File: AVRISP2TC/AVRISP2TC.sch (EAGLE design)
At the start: 14 parts, among them U1 NCP1117LPST33T3G

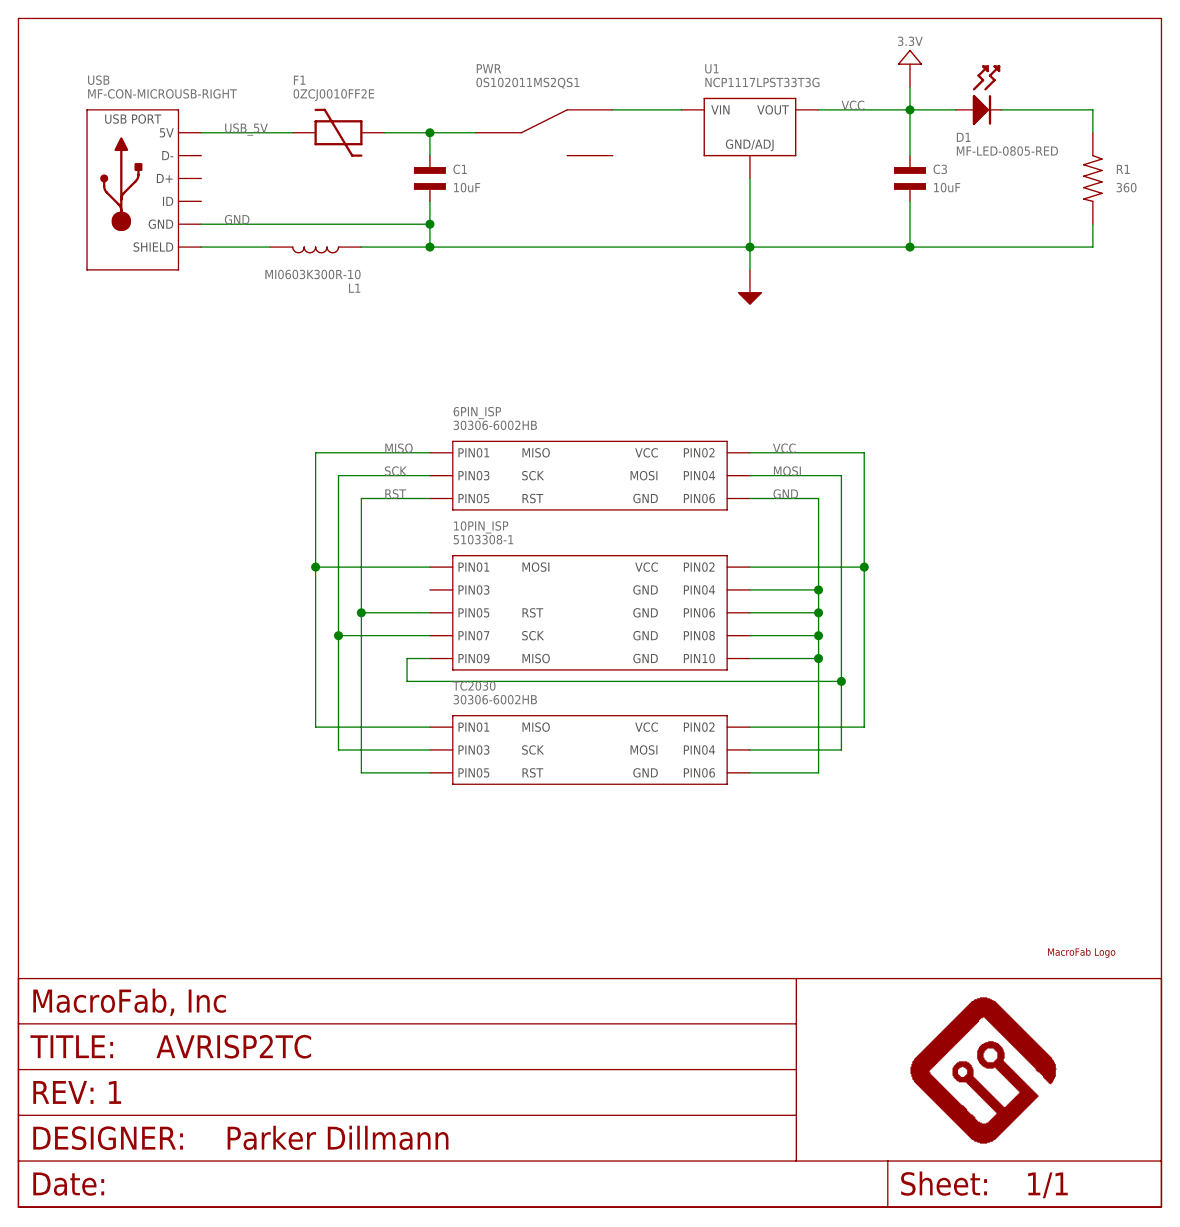
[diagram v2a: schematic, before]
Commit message: Fixed MISO/MOSI swap on 10Pin ISP header.
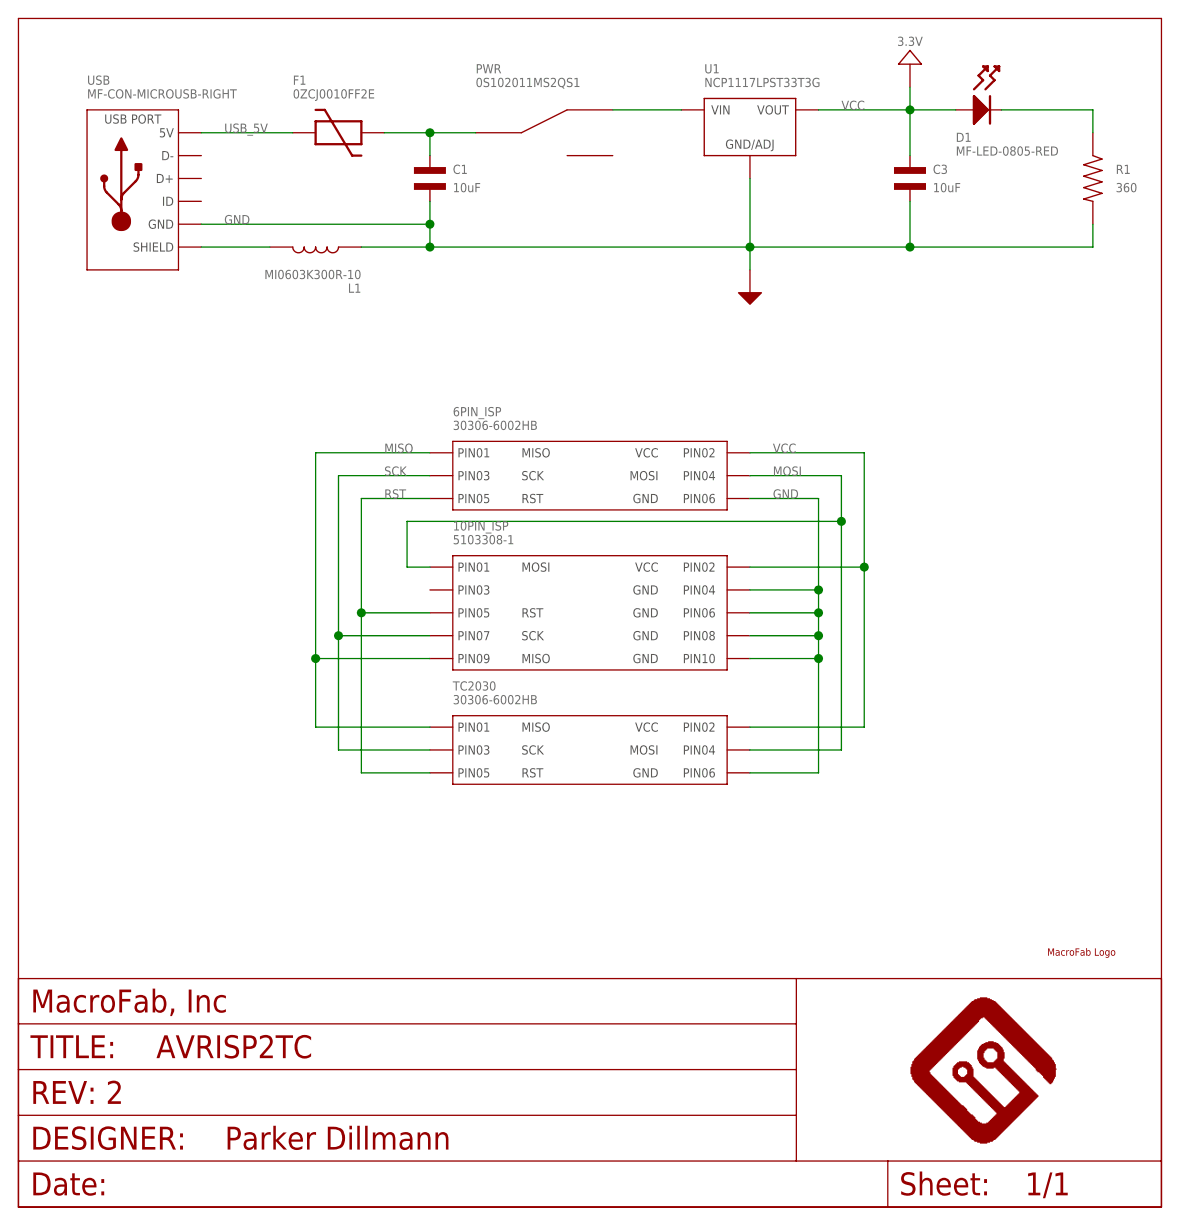
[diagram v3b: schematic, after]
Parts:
- FRAME1: REVNUM REV: 1 -> REV: 2
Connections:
- net MISO: now also 10PIN_ISP.PIN9; no longer 10PIN_ISP.PIN1
- net MOSI: now also 10PIN_ISP.PIN1; no longer 10PIN_ISP.PIN9
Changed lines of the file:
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@@
 <part name="FRAME1" library="MF_Aesthetics" deviceset="MF_FRAME" device="DEFAULT" value="">
 <attribute name="DNAME" value="Parker Dillmann"/>
-<attribute name="REVNUM" value="REV: 1"/>
+<attribute name="REVNUM" value="REV: 2"/>
 </part>
 <part name="U$1" library="MF_Aesthetics" deviceset="GND_RAIL" device=""/>
@@
 <pinref part="6PIN_ISP" gate="G$1" pin="PIN1"/>
 <wire x1="45.72" y1="58.42" x2="33.02" y2="58.42" width="0.1524" layer="91"/>
-<wire x1="33.02" y1="58.42" x2="33.02" y2="45.72" width="0.1524" layer="91"/>
 <pinref part="TC2030" gate="G$1" pin="PIN1"/>
-<wire x1="33.02" y1="45.72" x2="33.02" y2="27.94" width="0.1524" layer="91"/>
+<wire x1="33.02" y1="58.42" x2="33.02" y2="35.56" width="0.1524" layer="91"/>
+<wire x1="33.02" y1="35.56" x2="33.02" y2="27.94" width="0.1524" layer="91"/>
 <wire x1="33.02" y1="27.94" x2="45.72" y2="27.94" width="0.1524" layer="91"/>
-<pinref part="10PIN_ISP" gate="G$1" pin="PIN1"/>
-<wire x1="45.72" y1="45.72" x2="33.02" y2="45.72" width="0.1524" layer="91"/>
-<junction x="33.02" y="45.72"/>
 <label x="40.64" y="58.42" size="1.016" layer="95" font="vector"/>
+<pinref part="10PIN_ISP" gate="G$1" pin="PIN9"/>
+<wire x1="45.72" y1="35.56" x2="33.02" y2="35.56" width="0.1524" layer="91"/>
+<junction x="33.02" y="35.56"/>
 </segment>
 </net>
@@
 <pinref part="TC2030" gate="G$1" pin="PIN4"/>
 <wire x1="81.28" y1="25.4" x2="91.44" y2="25.4" width="0.1524" layer="91"/>
-<wire x1="91.44" y1="25.4" x2="91.44" y2="33.02" width="0.1524" layer="91"/>
 <pinref part="6PIN_ISP" gate="G$1" pin="PIN4"/>
-<wire x1="91.44" y1="33.02" x2="91.44" y2="55.88" width="0.1524" layer="91"/>
+<wire x1="91.44" y1="25.4" x2="91.44" y2="50.8" width="0.1524" layer="91"/>
+<wire x1="91.44" y1="50.8" x2="91.44" y2="55.88" width="0.1524" layer="91"/>
 <wire x1="91.44" y1="55.88" x2="81.28" y2="55.88" width="0.1524" layer="91"/>
-<pinref part="10PIN_ISP" gate="G$1" pin="PIN9"/>
-<wire x1="45.72" y1="35.56" x2="43.18" y2="35.56" width="0.1524" layer="91"/>
-<wire x1="43.18" y1="35.56" x2="43.18" y2="33.02" width="0.1524" layer="91"/>
-<wire x1="43.18" y1="33.02" x2="91.44" y2="33.02" width="0.1524" layer="91"/>
-<junction x="91.44" y="33.02"/>
 <label x="83.82" y="55.88" size="1.016" layer="95" font="vector"/>
-</segment>
-</net>
+<pinref part="10PIN_ISP" gate="G$1" pin="PIN1"/>
+<wire x1="45.72" y1="45.72" x2="43.18" y2="45.72" width="0.1524" layer="91"/>
+<wire x1="43.18" y1="45.72" x2="43.18" y2="50.8" width="0.1524" layer="91"/>
+<wire x1="43.18" y1="50.8" x2="91.44" y2="50.8" width="0.1524" layer="91"/>
+<junction x="91.44" y="50.8"/>
+</segment>
+</net>
